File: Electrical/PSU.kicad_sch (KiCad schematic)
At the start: 129 parts, among them J15 Conn_01x03_Pin, J16 USB_C_Receptacle_USB2.0, Q10 2N7002, Q11 SSM3J332R,LF, Q12 SSM3J332R,LF, Q13 SSM3J332R,LF, Q14 SSM3J332R,LF, Q5 2N7002, Q6 2N7002, Q7 NCE30P28Q, Q8 2N7002, Q9 2N7002, SW1 SW_Push, U12 SY8253ADC, U13 HT7533, U14 CH224Q_C46061833, U15 SY8253ADC, U16 SY8253ADC, U6 TL431DBZ, U7 SY8253ADC

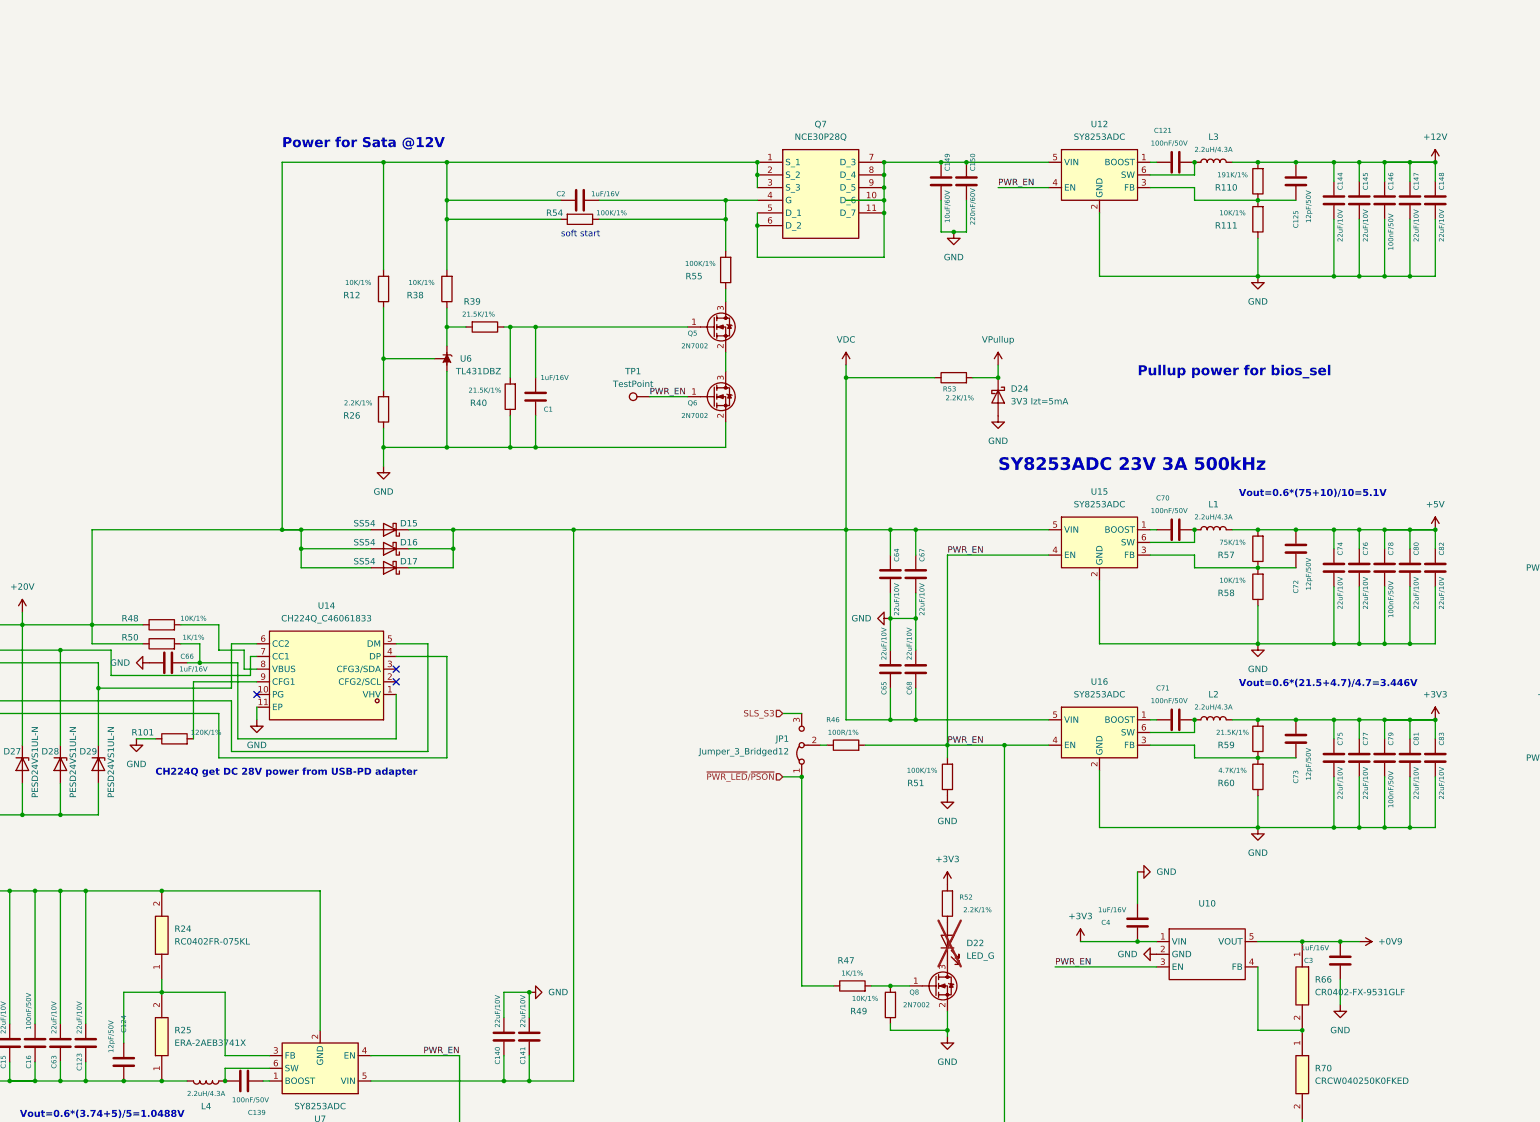
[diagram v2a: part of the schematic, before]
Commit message: replace the 12v buck with a 12 amp capable buck
also removed soft start circuit because its built in the Buck Converter IC
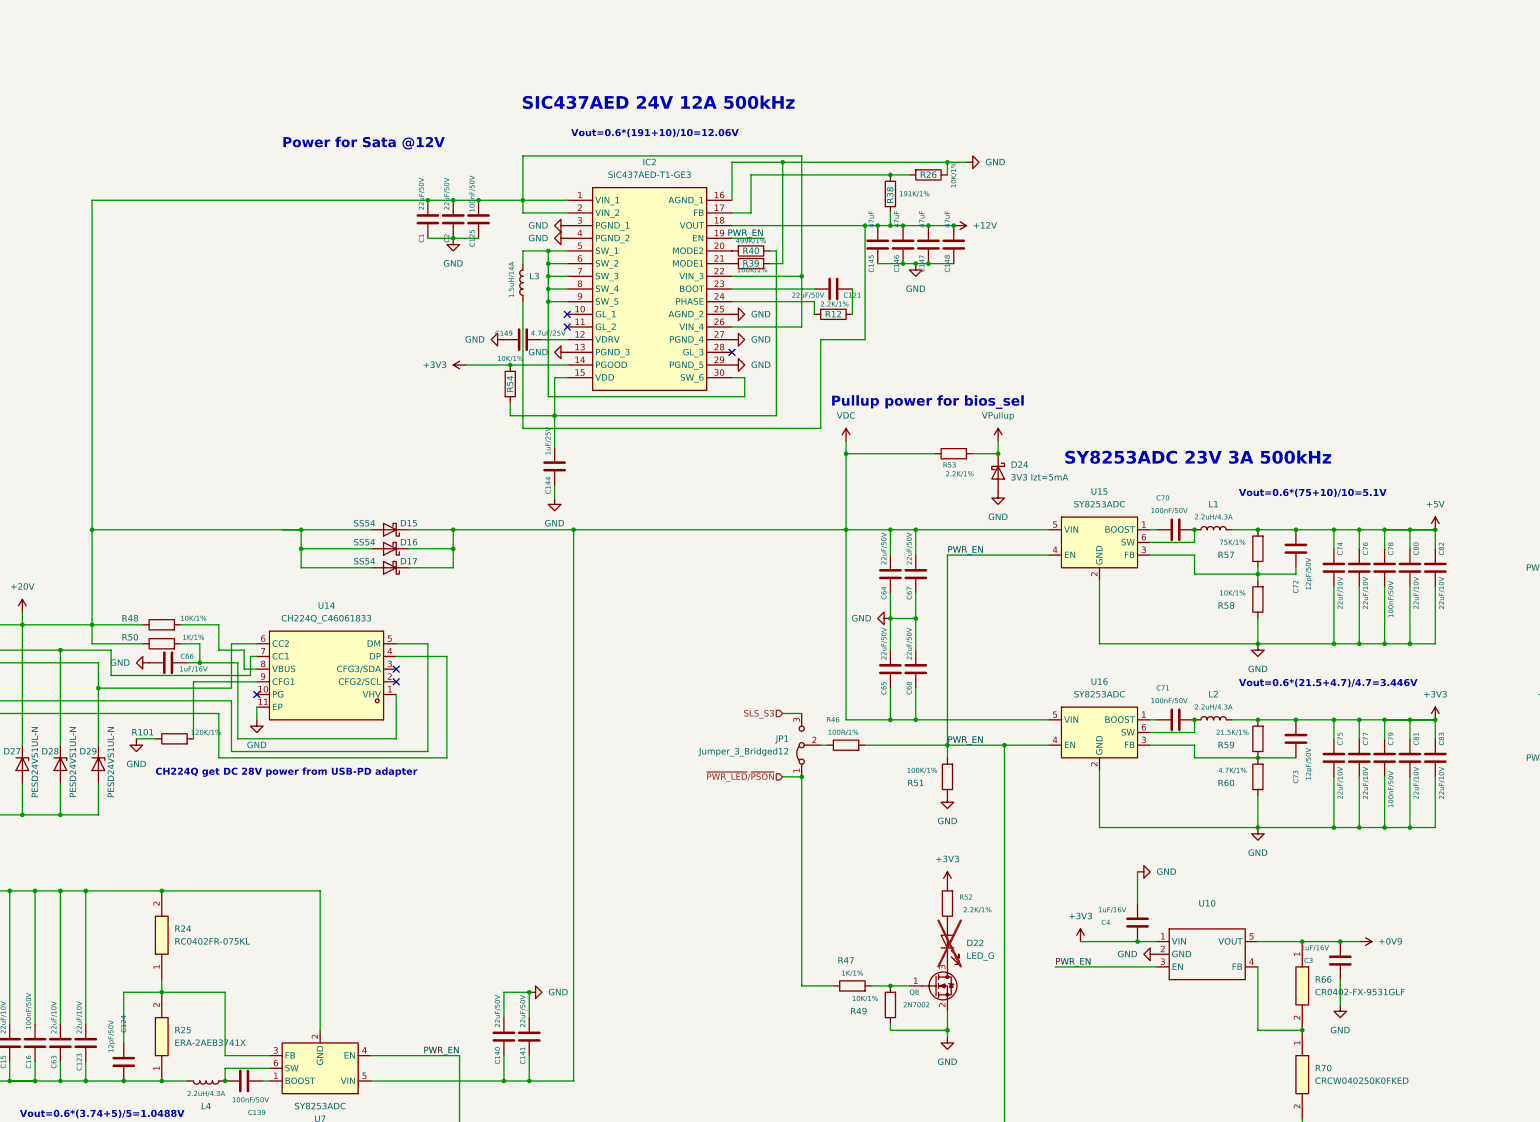
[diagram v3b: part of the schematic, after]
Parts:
- removed C150: 220nF/60V, A_HDJ_Library:C_0603_1608Metric, symbol Device:C
- removed Q5, Q6: 2N7002, A_HDJ_Library:SOT-23, symbol Transistor_FET:2N7002
- removed Q7: NCE30P28Q, A_HDJ_Library:MOSFET_PDFN8_3.3x3.3, symbol A_HDJ_Library:AON7262E
- removed R110: 191K/1%, A_HDJ_Library:R_0603_1608Metric, symbol Device:R
- removed R111: 10K/1%, A_HDJ_Library:R_0402_1005Metric, symbol Device:R
- removed R55: 100K/1%, A_HDJ_Library:R_0402_1005Metric, symbol Device:R
- removed TP1: TestPoint, A_HDJ_Library:TestPoint_Pad_D1.5mm, symbol Connector:TestPoint
- removed U12: SY8253ADC, Package_TO_SOT_SMD:TSOT-23-6, symbol Regulator_Switching:LM2734X
- removed U6: TL431DBZ, A_HDJ_Library:SOT-23, symbol Reference_Voltage:TL431DBZ
- added IC2: SiC437AED-T1-GE3, 28v buck:SIC437DEDT1GE3, symbol 28v buck:SiC437AED-T1-GE3
- C1, C2: value 1uF/16V -> 22uF/50V; footprint A_HDJ_Library:C_0402_1005Metric -> A_HDJ_Library:C_0603_1608Metric; SCH_Show_Footprint C0402 -> C603
- C121: value 100nF/50V -> 22uF/50V; footprint A_HDJ_Library:C_0402_1005Metric -> A_HDJ_Library:C_0603_1608Metric; SCH_Show_Footprint C0402 -> C603
- C125: value 12pF/50V -> 100nF/50V; footprint Capacitor_SMD:C_0402_1005Metric -> A_HDJ_Library:C_0603_1608Metric; SCH_Show_Footprint C0402 -> C603
- C140, C141, C64, C65, C67, C68: value 22uF/10V -> 22uF/50V
- C144: value 22uF/10V -> 1uF/25V; footprint A_HDJ_Library:C_0603_1608Metric -> A_HDJ_Library:C_0402_1005Metric
- C145, C147, C148: value 22uF/10V -> 47uF; footprint A_HDJ_Library:C_0603_1608Metric -> A_HDJ_Library:C_0402_1005Metric
- C146: value 100nF/50V -> 47uF; SCH_Show_Footprint C0402 -> C603
- C149: value 10uF/60V -> 4.7uF/25V; footprint A_HDJ_Library:C_0603_1608Metric -> A_HDJ_Library:C_0402_1005Metric
- L3: value 2.2uH/4.3A -> 1.5uH/14A
- R12: value 10K/1% -> 2.2K/1%
- R26: value 2.2K/1% -> 10K/1%
- R38: value 10K/1% -> 191K/1%
- R39: value 21.5K/1% -> 100K/1%
- R40: value 21.5K/1% -> 499K/1%
- R54: value 100K/1% -> 10K/1%
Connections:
- net +12V: now also C145.1, C147.1, C148.1, L3.1, R38.2, IC2.18 (VOUT); no longer C125.1, C144.2, C145.2, C147.2, C148.2, L3.2
- net +20V: now also C1.1, C125.1, C2.1, IC2.1 (VIN_1), IC2.2 (VIN_2), IC2.22 (VIN_3), IC2.26 (VIN_4); no longer C2.2, R12.2, R38.2, R54.2
- net +3V3: now also R54.1, IC2.14 (PGOOD)
- net GND: now also C125.2, C144.2, C145.2, C147.2, C148.2, C149.2, C2.2, C64.2, C67.2, R39.1, IC2.13 (PGND_3), IC2.16 (AGND_1), IC2.25 (AGND_2), IC2.27 (PGND_4), IC2.29 (PGND_5), IC2.3 (PGND_1), IC2.4 (PGND_2); no longer C144.1, C145.1, C147.1, C148.1, C149.1, C64.1, C67.1, R40.1
- net PWR_EN: now also IC2.19 (EN)
- net VDC: now also C64.1, C67.1; no longer C64.2, C67.2
- net at C121.1: now also IC2.23 (BOOT); no longer L3.1
- net at C121.2: now also R12.1
- net at R26.2: now also R38.1, IC2.17 (FB); no longer R12.1
- net at R39.2: now also IC2.21 (MODE1); no longer R38.1
- new net: C144.1, IC2.15 (VDD), R40.1, R54.2
- new net: C149.1, IC2.12 (VDRV)
- new net: IC2.20 (MODE2), R40.2
- new net: IC2.24 (PHASE), R12.2
- new net: IC2.30 (SW_6), IC2.5 (SW_1), IC2.6 (SW_2), IC2.7 (SW_3), IC2.8 (SW_4), IC2.9 (SW_5), L3.2
- no-connect marks 5 -> 8
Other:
- note added: "SIC437AED 24V 12A 500kHz"
- note added: "Vout=0.6*(191+10)/10=12.06V"
- note removed: "soft start"
- moved on the sheet: D24, R53, R58

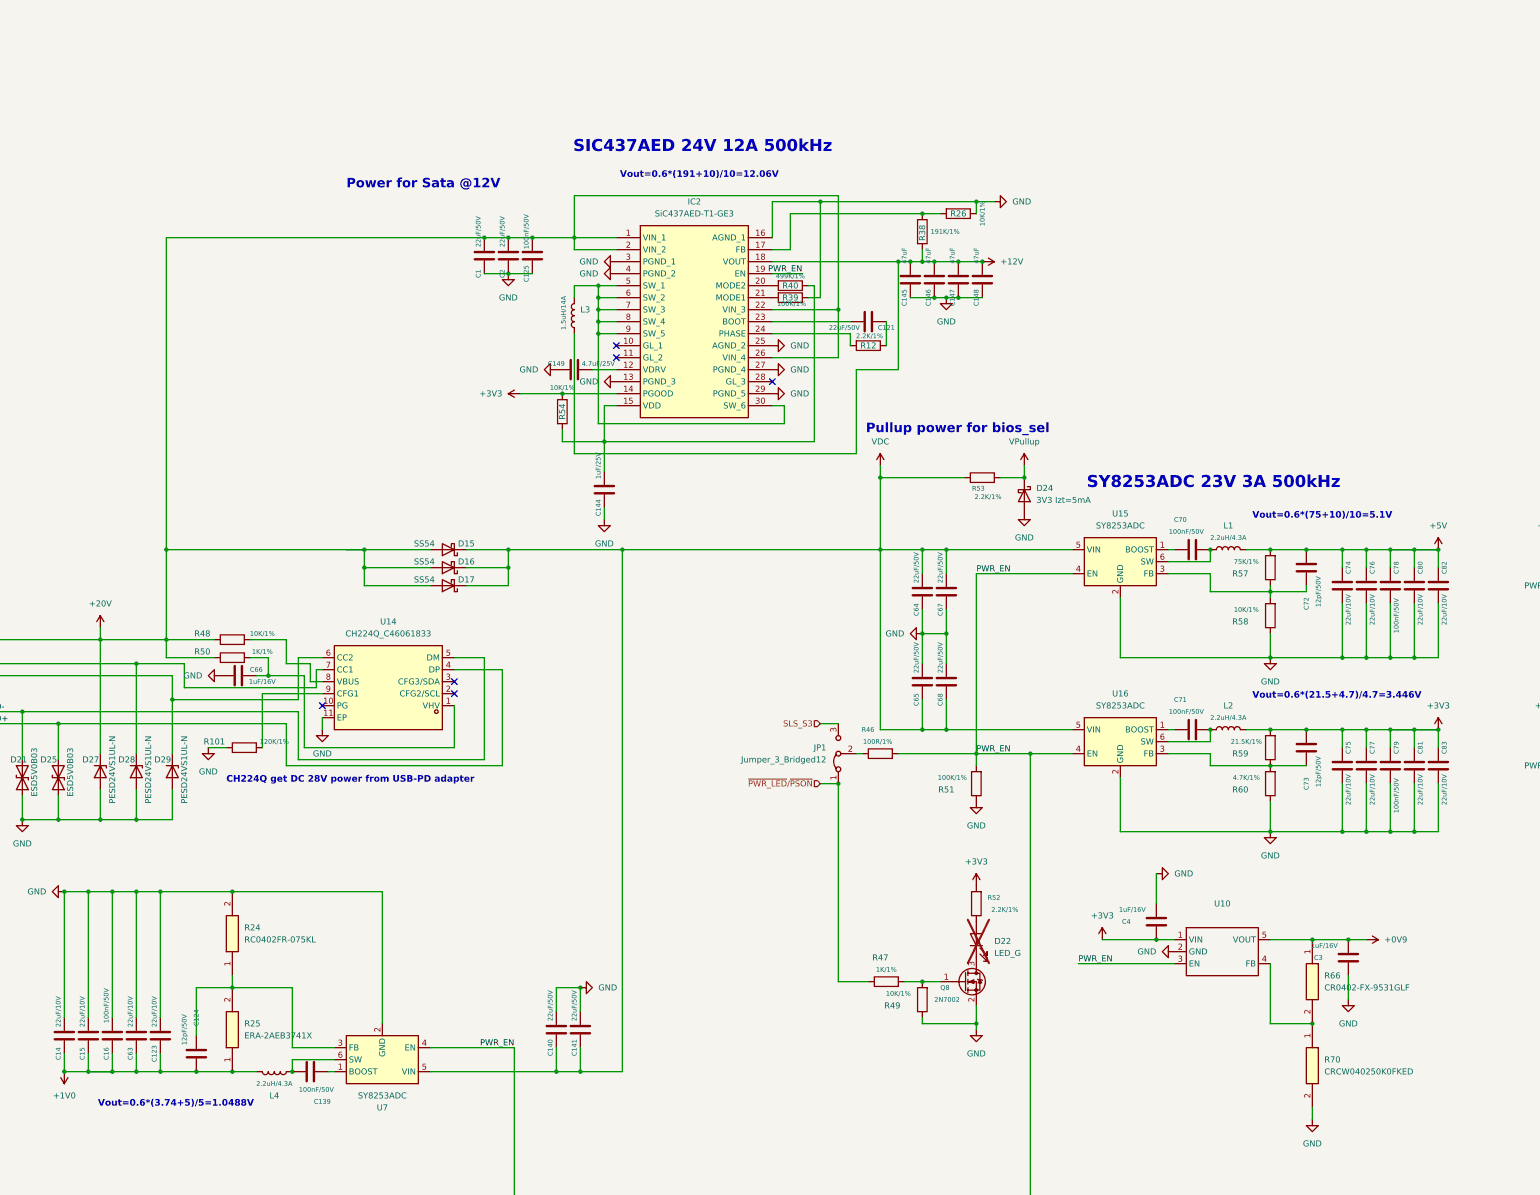
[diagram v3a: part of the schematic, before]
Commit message: Add step down converter
Prevent 20v going into the lattepanda mu, it has been stepped down to 15v
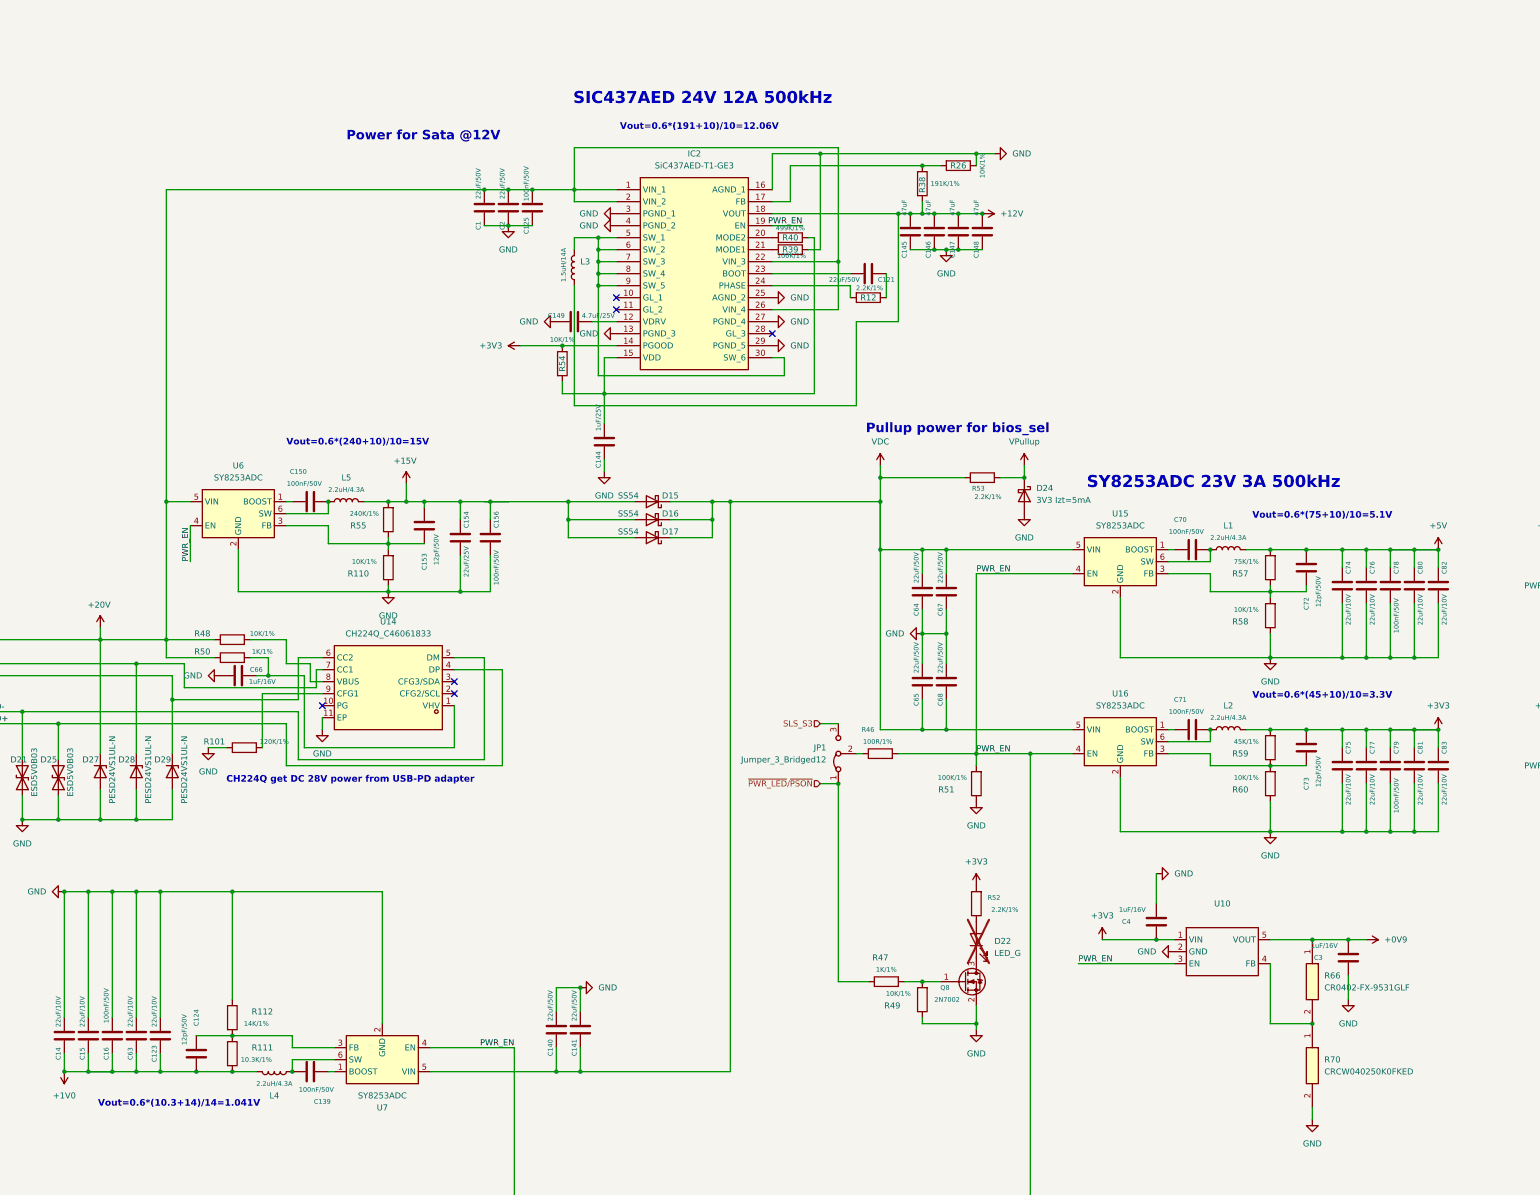
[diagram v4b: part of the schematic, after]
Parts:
- removed R24: RC0402FR-075KL, Resistor_SMD:R_0402_1005Metric, symbol 5k:RC0402FR-075KL
- removed R25: ERA-2AEB3741X, A_HDJ_Library:R_0402_1005Metric, symbol 3.74k resis:ERA-2AEB3741X
- added C150, C156: 100nF/50V, A_HDJ_Library:C_0402_1005Metric, symbol Device:C
- added C153: 12pF/50V, Capacitor_SMD:C_0402_1005Metric, symbol Device:C
- added C154: 22uF/25V, A_HDJ_Library:C_0603_1608Metric, symbol Device:C
- added L5: 2.2uH/4.3A, A_HDJ_Library:L_Sunlord_SWPA4020S, symbol Device:L
- added R110: 10K/1%, A_HDJ_Library:R_0402_1005Metric, symbol Device:R
- added R111: 10.3K/1%, A_HDJ_Library:R_0402_1005Metric, symbol Device:R
- added R112: 14K/1%, A_HDJ_Library:R_0402_1005Metric, symbol Device:R
- added R55: 240K/1%, A_HDJ_Library:R_0402_1005Metric, symbol Device:R
- added U6: SY8253ADC, Package_TO_SOT_SMD:TSOT-23-6, symbol Regulator_Switching:LM2734X
- R59: value 21.5K/1% -> 45K/1%
- R60: value 4.7K/1% -> 10K/1%
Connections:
- net +1V0: now also R111.2
- net +20V: now also U6.5 (VIN); no longer D15.2 (A), D16.2 (A), D17.2 (A)
- net GND: now also C154.1, C156.2, R110.1, R112.1, U6.2 (GND)
- net PWR_EN: now also U6.4 (EN)
- net at C124.2, U7.3 (FB): now also R111.1, R112.2
- new net: C153.2, R110.2, R55.1, U6.3 (FB)
- new net: C150.1, L5.1, U6.6 (SW)
- new net: C150.2, U6.1 (BOOST)
- new net +15V: C153.1, C154.2, C156.1, D15.2 (A), D16.2 (A), D17.2 (A), L5.2, R55.2
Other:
- note added: "Vout=0.6*(10.3+14)/14=1.041V"
- note added: "Vout=0.6*(240+10)/10=15V"
- note added: "Vout=0.6*(45+10)/10=3.3V"
- note removed: "Vout=0.6*(21.5+4.7)/4.7=3.446V"
- note removed: "Vout=0.6*(3.74+5)/5=1.0488V"
- moved on the sheet: C1, C121, C125, C144, C145, C146, C147, C148, C149, C2, D15, D16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
